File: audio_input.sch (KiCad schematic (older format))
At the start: 17 parts, among them U9 OPA1664

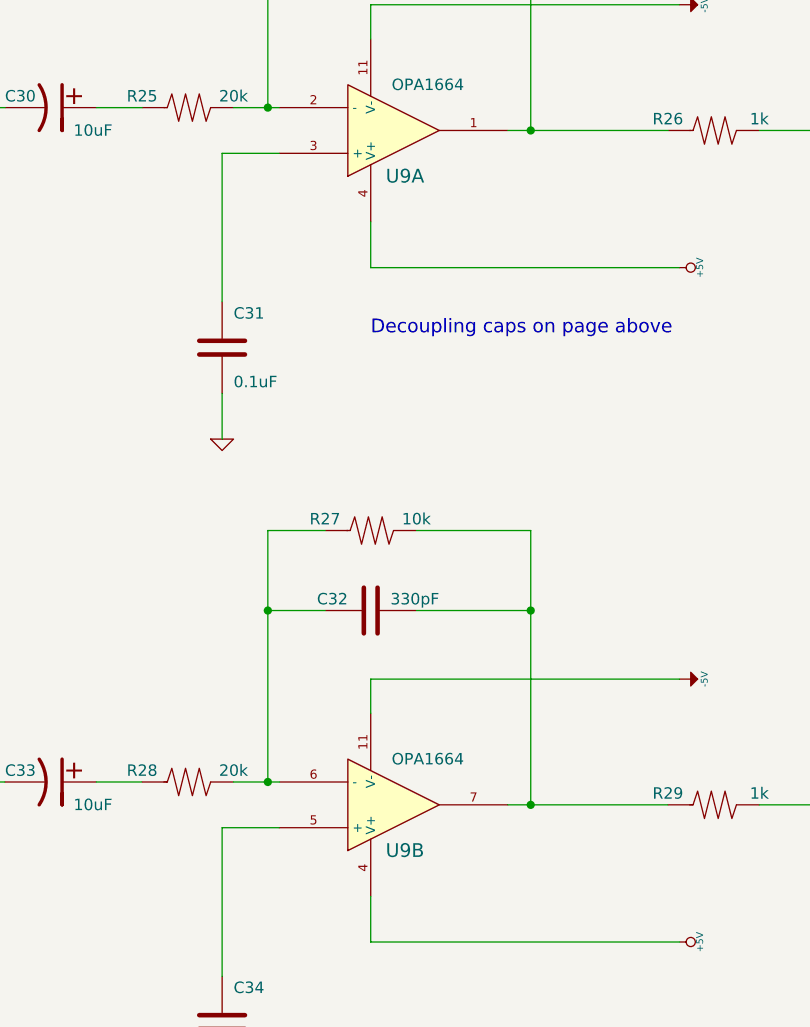
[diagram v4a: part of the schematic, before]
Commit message: Added EMI and ESD protection to audio interface, started assoc. footprints
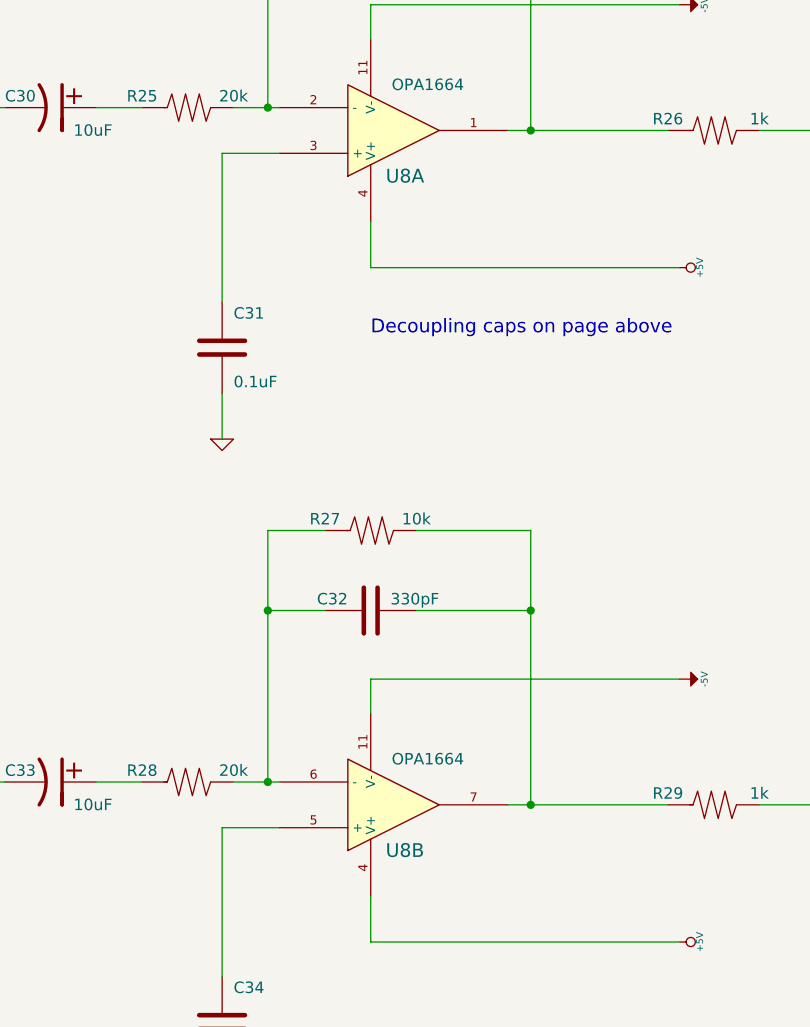
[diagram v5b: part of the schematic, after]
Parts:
- renumbered U9 to U8
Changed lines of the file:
@@
 $EndDescr
 $Comp
-L OPA1664 U9
+L OPA1664 U8
 U 1 1 5A49B619
 P 5100 2100
-F 0 "U9" H 5150 2300 60  0000 C CNN
+F 0 "U8" H 5150 2300 60  0000 C CNN
 F 1 "OPA1664" H 5250 1900 50  0000 C CNN
-F 2 "" H 5100 2100 60  0000 C CNN
+F 2 "" H 5100 2100 60  0001 C CNN
 F 3 "" H 5100 2100 60  0000 C CNN
 	1    5100 2100
@@
 	5000 1550 5000 1700
 $Comp
-L -5V #PWR075
+L -5V #PWR88
 U 1 1 5A49B7EA
 P 6350 1550
-F 0 "#PWR075" H 6350 1690 20  0001 C CNN
+F 0 "#PWR88" H 6350 1690 20  0001 C CNN
 F 1 "-5V" H 6350 1660 30  0000 C CNN
 F 2 "" H 6350 1550 60  0000 C CNN
@@
 F 0 "C29" V 5050 1350 50  0000 L CNN
 F 1 "330pF" V 5050 950 50  0000 L CNN
-F 2 "" H 5000 1250 60  0000 C CNN
+F 2 "" H 5000 1250 60  0001 C CNN
 F 3 "" H 5000 1250 60  0000 C CNN
 	1    5000 1250
@@
 F 0 "C30" V 3550 1800 50  0000 L CNN
 F 1 "10uF" V 3700 2100 50  0000 L CNN
-F 2 "" H 3600 2000 60  0000 C CNN
+F 2 "" H 3600 2000 60  0001 C CNN
 F 3 "" H 3600 2000 60  0000 C CNN
 	1    3600 2000
@@
 F 0 "C31" H 4400 3200 50  0000 L CNN
 F 1 "0.1uF" H 4400 2900 50  0000 L CNN
-F 2 "" H 4350 3050 60  0000 C CNN
+F 2 "" H 4350 3050 60  0001 C CNN
 F 3 "" H 4350 3050 60  0000 C CNN
 	1    4350 3050
@@
 F 0 "R24" H 4800 950 50  0000 C CNN
 F 1 "10k" H 5200 950 50  0000 C CNN
-F 2 "" H 5000 900 60  0000 C CNN
+F 2 "" H 5000 900 60  0001 C CNN
 F 3 "" H 5000 900 60  0000 C CNN
 	1    5000 900
@@
 Connection ~ 5700 1250
 $Comp
-L GND #PWR076
+L GND #PWR90
 U 1 1 5A49BD8E
 P 4350 3450
-F 0 "#PWR076" H 4350 3450 30  0001 C CNN
+F 0 "#PWR90" H 4350 3450 30  0001 C CNN
 F 1 "GND" H 4350 3380 30  0001 C CNN
 F 2 "" H 4350 3450 60  0000 C CNN
@@
 F 0 "R25" H 4000 2050 50  0000 C CNN
 F 1 "20k" H 4400 2050 50  0000 C CNN
-F 2 "" H 4200 2000 60  0000 C CNN
+F 2 "" H 4200 2000 60  0001 C CNN
 F 3 "" H 4200 2000 60  0000 C CNN
 	1    4200 2000
@@
 F 0 "R26" H 6300 2150 50  0000 C CNN
 F 1 "1k" H 6700 2150 50  0000 C CNN
-F 2 "" H 6500 2100 60  0000 C CNN
+F 2 "" H 6500 2100 60  0001 C CNN
 F 3 "" H 6500 2100 60  0000 C CNN
 	1    6500 2100
@@
 	7150 3450 7150 3250
 $Comp
-L GND #PWR077
+L GND #PWR91
 U 1 1 5A49C264
 P 7150 3450
-F 0 "#PWR077" H 7150 3450 30  0001 C CNN
+F 0 "#PWR91" H 7150 3450 30  0001 C CNN
 F 1 "GND" H 7150 3380 30  0001 C CNN
 F 2 "" H 7150 3450 60  0000 C CNN
@@
 F 0 "D3" H 7150 3150 40  0000 C CNN
 F 1 "DIODE" H 7150 2950 40  0000 C CNN
-F 2 "" H 7150 3050 60  0000 C CNN
+F 2 "" H 7150 3050 60  0001 C CNN
 F 3 "" H 7150 3050 60  0000 C CNN
 	1    7150 3050
@@
 F 0 "D2" H 7150 1300 40  0000 C CNN
 F 1 "DIODE" H 7150 1100 40  0000 C CNN
-F 2 "" H 7150 1200 60  0000 C CNN
+F 2 "" H 7150 1200 60  0001 C CNN
 F 3 "" H 7150 1200 60  0000 C CNN
 	1    7150 1200
@@
 $EndComp
 $Comp
-L +5V #PWR078
+L +5V #PWR87
 U 1 1 5A49C8EC
 P 7150 750
-F 0 "#PWR078" H 7150 840 20  0001 C CNN
+F 0 "#PWR87" H 7150 840 20  0001 C CNN
 F 1 "+5V" H 7150 840 30  0000 C CNN
 F 2 "" H 7150 750 60  0000 C CNN
@@
 ADC_VINL
 $Comp
-L OPA1664 U9
+L OPA1664 U8
 U 2 1 5A49EA75
 P 5100 5050
-F 0 "U9" H 5150 5250 60  0000 C CNN
+F 0 "U8" H 5150 5250 60  0000 C CNN
 F 1 "OPA1664" H 5250 4850 50  0000 C CNN
-F 2 "" H 5100 5050 60  0000 C CNN
+F 2 "" H 5100 5050 60  0001 C CNN
 F 3 "" H 5100 5050 60  0000 C CNN
 	2    5100 5050
@@
 	5000 4500 5000 4650
 $Comp
-L -5V #PWR079
+L -5V #PWR93
 U 1 1 5A49EA7F
 P 6350 4500
-F 0 "#PWR079" H 6350 4640 20  0001 C CNN
+F 0 "#PWR93" H 6350 4640 20  0001 C CNN
 F 1 "-5V" H 6350 4610 30  0000 C CNN
 F 2 "" H 6350 4500 60  0000 C CNN
@@
 $EndComp
 $Comp
-L +5V #PWR080
+L +5V #PWR94
 U 1 1 5A49EA85
 P 6350 5650
-F 0 "#PWR080" H 6350 5740 20  0001 C CNN
+F 0 "#PWR94" H 6350 5740 20  0001 C CNN
 F 1 "+5V" H 6350 5740 30  0000 C CNN
 F 2 "" H 6350 5650 60  0000 C CNN
@@
 F 0 "C32" V 5050 4300 50  0000 L CNN
 F 1 "330pF" V 5050 3900 50  0000 L CNN
-F 2 "" H 5000 4200 60  0000 C CNN
+F 2 "" H 5000 4200 60  0001 C CNN
 F 3 "" H 5000 4200 60  0000 C CNN
 	1    5000 4200
@@
 F 0 "C33" V 3550 4750 50  0000 L CNN
 F 1 "10uF" V 3700 5050 50  0000 L CNN
-F 2 "" H 3600 4950 60  0000 C CNN
+F 2 "" H 3600 4950 60  0001 C CNN
 F 3 "" H 3600 4950 60  0000 C CNN
 	1    3600 4950
@@
 F 0 "C34" H 4400 6150 50  0000 L CNN
 F 1 "0.1uF" H 4400 5850 50  0000 L CNN
-F 2 "" H 4350 6000 60  0000 C CNN
+F 2 "" H 4350 6000 60  0001 C CNN
 F 3 "" H 4350 6000 60  0000 C CNN
 	1    4350 6000
@@
 F 0 "R27" H 4800 3900 50  0000 C CNN
 F 1 "10k" H 5200 3900 50  0000 C CNN
-F 2 "" H 5000 3850 60  0000 C CNN
+F 2 "" H 5000 3850 60  0001 C CNN
 F 3 "" H 5000 3850 60  0000 C CNN
 	1    5000 3850
@@
 Connection ~ 5700 4200
 $Comp
-L GND #PWR081
+L GND #PWR95
 U 1 1 5A49EAC6
 P 4350 6400
-F 0 "#PWR081" H 4350 6400 30  0001 C CNN
+F 0 "#PWR95" H 4350 6400 30  0001 C CNN
 F 1 "GND" H 4350 6330 30  0001 C CNN
 F 2 "" H 4350 6400 60  0000 C CNN
@@
 F 0 "R28" H 4000 5000 50  0000 C CNN
 F 1 "20k" H 4400 5000 50  0000 C CNN
-F 2 "" H 4200 4950 60  0000 C CNN
+F 2 "" H 4200 4950 60  0001 C CNN
 F 3 "" H 4200 4950 60  0000 C CNN
 	1    4200 4950
@@
 F 0 "R29" H 6300 5100 50  0000 C CNN
 F 1 "1k" H 6700 5100 50  0000 C CNN
-F 2 "" H 6500 5050 60  0000 C CNN
+F 2 "" H 6500 5050 60  0001 C CNN
 F 3 "" H 6500 5050 60  0000 C CNN
 	1    6500 5050
@@
 	7150 6400 7150 6200
 $Comp
-L GND #PWR082
+L GND #PWR96
 U 1 1 5A49EAF1
 P 7150 6400
-F 0 "#PWR082" H 7150 6400 30  0001 C CNN
+F 0 "#PWR96" H 7150 6400 30  0001 C CNN
 F 1 "GND" H 7150 6330 30  0001 C CNN
 F 2 "" H 7150 6400 60  0000 C CNN
@@
 F 0 "D5" H 7150 6100 40  0000 C CNN
 F 1 "DIODE" H 7150 5900 40  0000 C CNN
-F 2 "" H 7150 6000 60  0000 C CNN
+F 2 "" H 7150 6000 60  0001 C CNN
 F 3 "" H 7150 6000 60  0000 C CNN
 	1    7150 6000
@@
 F 0 "D4" H 7150 4250 40  0000 C CNN
 F 1 "DIODE" H 7150 4050 40  0000 C CNN
-F 2 "" H 7150 4150 60  0000 C CNN
+F 2 "" H 7150 4150 60  0001 C CNN
 F 3 "" H 7150 4150 60  0000 C CNN
 	1    7150 4150
@@
 $EndComp
 $Comp
-L +5V #PWR083
+L +5V #PWR92
 U 1 1 5A49EB03
 P 7150 3700
-F 0 "#PWR083" H 7150 3790 20  0001 C CNN
+F 0 "#PWR92" H 7150 3790 20  0001 C CNN
 F 1 "+5V" H 7150 3790 30  0000 C CNN
 F 2 "" H 7150 3700 60  0000 C CNN
@@
 	5000 2700 6350 2700
 $Comp
-L +5V #PWR084
+L +5V #PWR89
 U 1 1 5A49B806
 P 6350 2700
-F 0 "#PWR084" H 6350 2790 20  0001 C CNN
+F 0 "#PWR89" H 6350 2790 20  0001 C CNN
 F 1 "+5V" H 6350 2790 30  0000 C CNN
 F 2 "" H 6350 2700 60  0000 C CNN
